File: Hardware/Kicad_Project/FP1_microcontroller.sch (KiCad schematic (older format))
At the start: 1 part

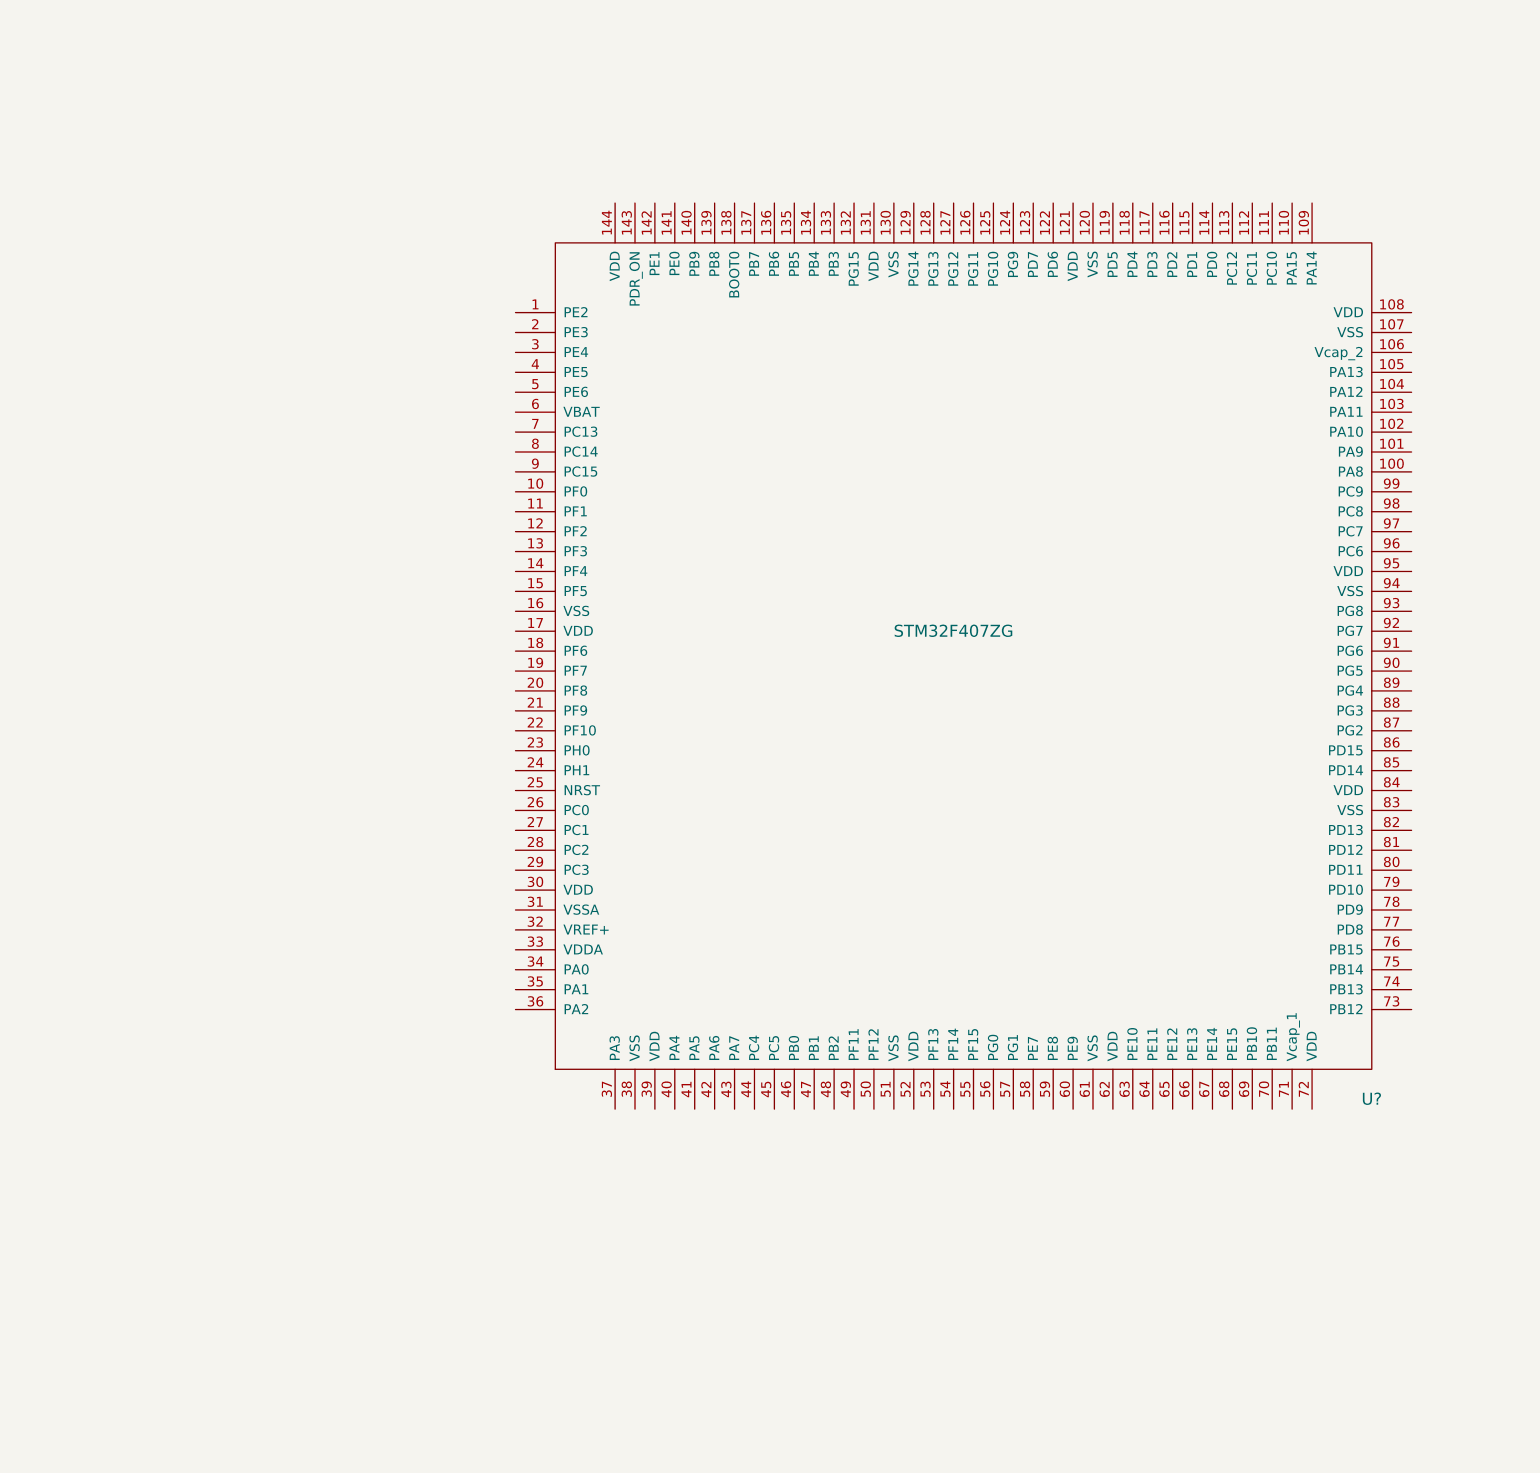
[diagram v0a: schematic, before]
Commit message: [HARD] Minimal STM32F407ZG circuitry
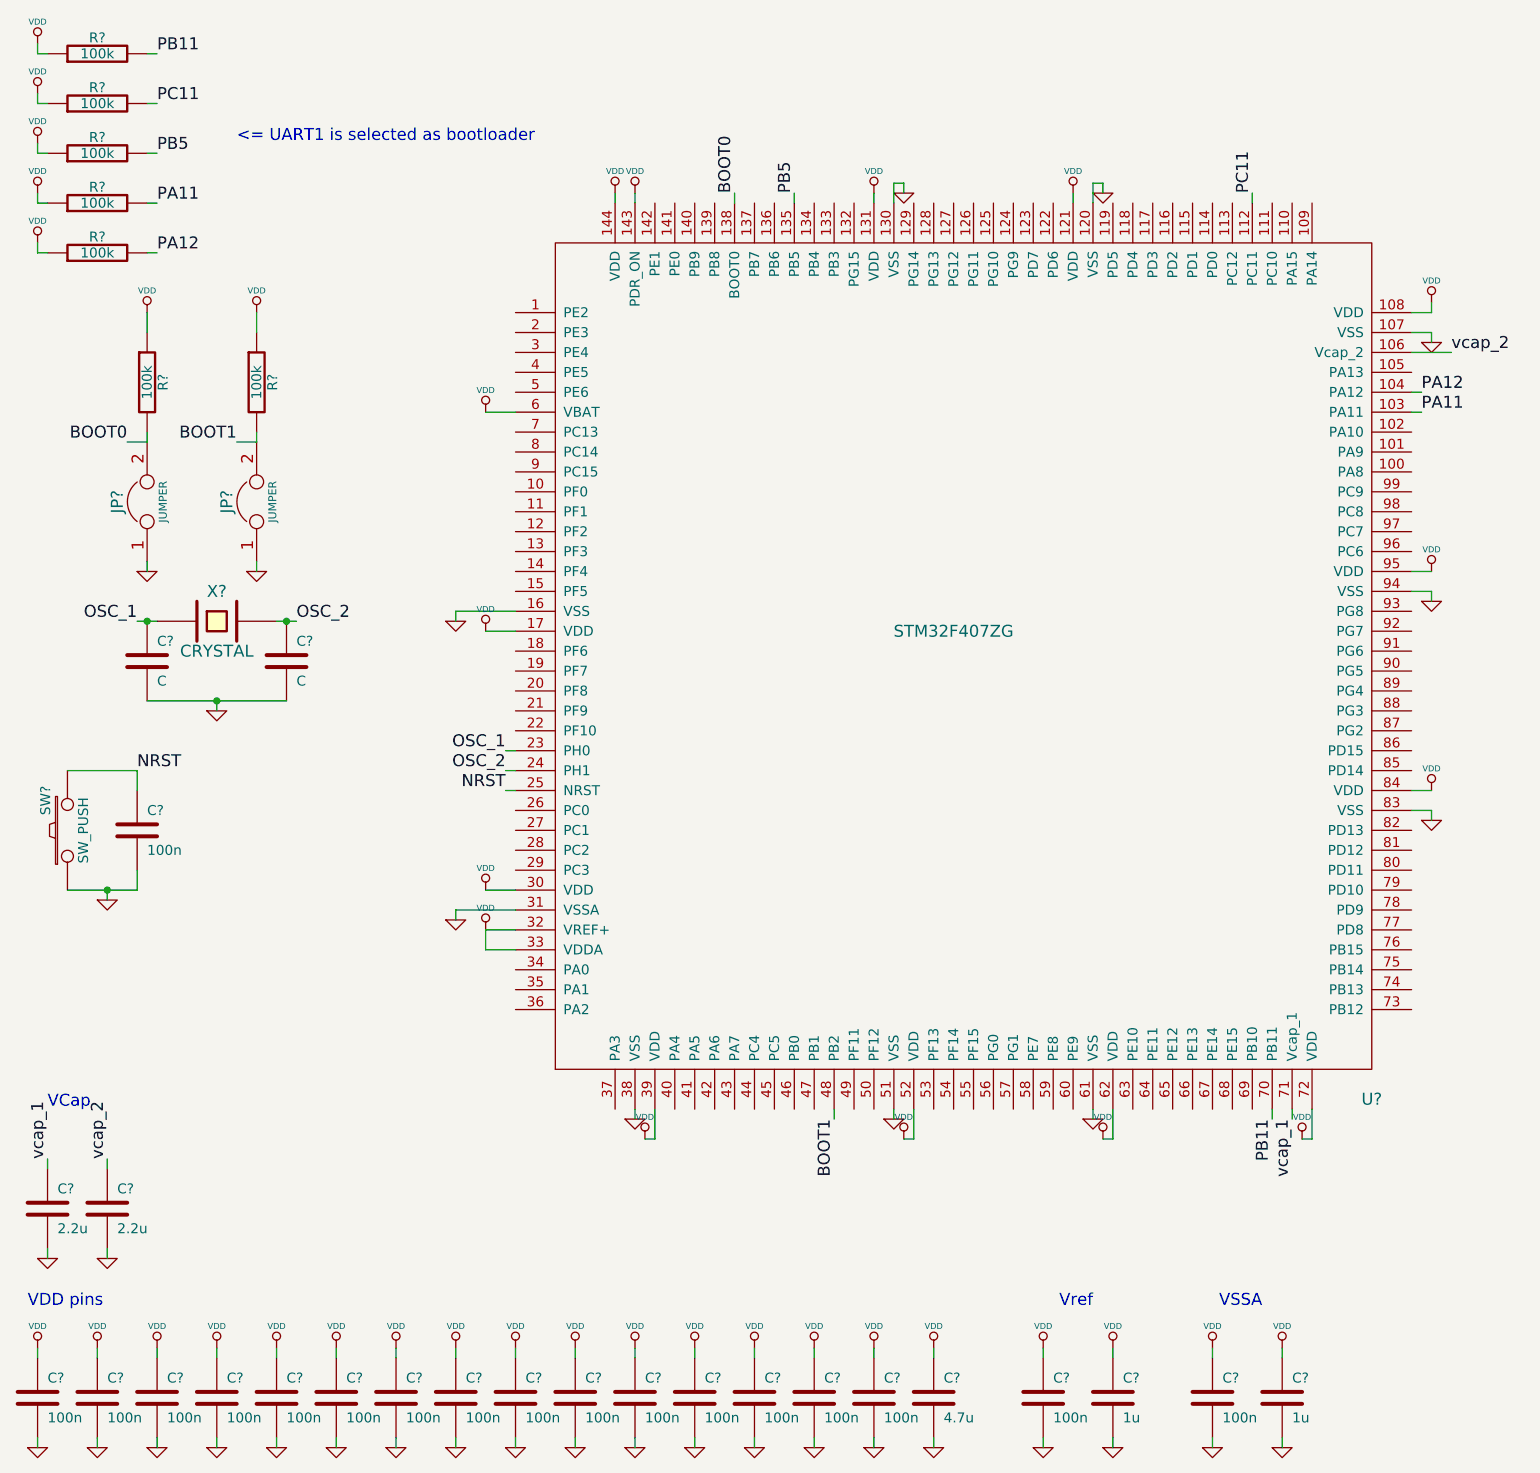
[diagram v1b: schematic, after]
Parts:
- added C? (x18): 100n, symbol C
- added C?: 4.7u, symbol C
- added C? (x2): 2.2u, symbol C
- added C? (x2): 1u, symbol C
- added C? (x2): C, symbol C
- added JP? (x2): JUMPER, symbol JUMPER
- added R? (x7): 100k, symbol R
- added SW?: SW_PUSH, symbol SW_PUSH
- added X?: CRYSTAL, symbol CRYSTAL
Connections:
- net PA11: now reaches U?.103 (PA11)
- net PA11: now also R?.2
- net PA12: now reaches U?.104 (PA12)
- net PA12: now also R?.2
- net vcap_2: now reaches U?.106 (Vcap_2)
- net vcap_2: now also C?.1
- net GND: now reaches U?.107 (VSS)
- net GND: now also U?.120 (VSS), U?.130 (VSS), U?.16 (VSS), U?.31 (VSSA), U?.38 (VSS), U?.51 (VSS), U?.61 (VSS), U?.83 (VSS), U?.94 (VSS), C?.2, C?.2, C?.2, C?.2, C?.2, C?.2, C?.2, C?.2, C?.2, C?.2, C?.2, C?.2, C?.2, C?.2, C?.2, C?.2, C?.2, C?.2, C?.2, C?.2, C?.2, C?.2, C?.2, C?.2, C?.2, JP?.1, JP?.1, SW?.1
- net VDD: now reaches U?.108 (VDD)
- net VDD: now also U?.121 (VDD), U?.131 (VDD), U?.143 (PDR_ON), U?.144 (VDD), U?.17 (VDD), U?.30 (VDD), U?.32 (VREF+), U?.33 (VDDA), U?.39 (VDD), U?.52 (VDD), U?.6 (VBAT), U?.62 (VDD), U?.72 (VDD), U?.84 (VDD), U?.95 (VDD), C?.1, C?.1, C?.1, C?.1, C?.1, C?.1, C?.1, C?.1, C?.1, C?.1, C?.1, C?.1, C?.1, C?.1, C?.1, C?.1, C?.1, C?.1, C?.1, C?.1, R?.1, R?.1, R?.1, R?.1, R?.1, R?.1, R?.1
- net PC11: now reaches U?.112 (PC11)
- net PC11: now also R?.2
- net PB5: now reaches U?.135 (PB5)
- net PB5: now also R?.2
- net BOOT0: now reaches U?.138 (BOOT0)
- net BOOT0: now also JP?.2, R?.2
- net OSC_1: now reaches U?.23 (PH0)
- net OSC_1: now also C?.1, X?.1
- net OSC_2: now reaches U?.24 (PH1)
- net OSC_2: now also C?.1, X?.2
- net NRST: now reaches U?.25 (NRST)
- net NRST: now also C?.1, SW?.2
- net BOOT1: now reaches U?.48 (PB2)
- net BOOT1: now also JP?.2, R?.2
- net PB11: now reaches U?.70 (PB11)
- net PB11: now also R?.2
- net vcap_1: now reaches U?.71 (Vcap_1)
- net vcap_1: now also C?.1
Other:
- note added: "<= UART1 is selected as bootloader"
- note added: "VCap"
- note added: "VDD pins"
- note added: "VSSA"
- note added: "Vref"
